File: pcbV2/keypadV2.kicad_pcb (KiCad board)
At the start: 2 copper layers, 73 parts, among them J1 Conn_01x02_Female, J2 USB_C_Receptacle, J3 Conn_01x03_Male, Q1 Q_NMOS_GSD, SW1 SW_Push, SW10 SW_Push, SW11 SW_Push, SW12 SW_Push, SW13 SW_SPDT, SW14 SW_Push, SW15 SW_Push, SW16 SW_Push, SW17 SW_DIP_x03, SW2 SW_Push, SW3 SW_Push, SW4 SW_Push, SW5 SW_Push, SW6 SW_Push, SW7 SW_Push, SW8 SW_Push, SW9 SW_Push, U1 Teensy4.0, U2 Waveshare_OLED_RGB

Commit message: remade teensy footprint
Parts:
- J2: moved to B.Cu
- U1: footprint teensy:Teensy40 -> teensy:Teensy40_REDUCED_PINS
- moved C13 148.5 mm to (264.5, 136.4)
- moved C8 148.5 mm to (258.5, 163.0)
- moved D13 148.5 mm to (258.6, 136.5)
- moved D21 148.5 mm to (259.8, 158.0)
- moved D9 148.5 mm to (279.4, 164.0)
- moved SW13 148.5 mm to (253.2, 157.0)
- moved SW16 148.5 mm to (280.8, 156.8)
- moved SW17 148.5 mm to (272.7, 157.5)
- moved SW10 147.9 mm to (111.3, 178.3)
- moved SW2 122.0 mm to (91.4, 137.7)
- moved SW6 120.8 mm to (111.3, 157.5)
- moved SW11 99.8 mm to (131.1, 178.3)
- moved J2 97.0 mm to (130.3, 113.8)
- moved SW1 91.7 mm to (91.4, 117.9)
- moved J1 77.7 mm to (132.8, 119.4), turned to 90 degrees
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
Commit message: basic layout v1
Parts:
- D1, D10, D11, D12, D2, D3, D4, D5, D6, D7, D8, D9, J1, SW14, SW15, SW16, SW17: moved to B.Cu
- moved SW13 219.6 mm to (34.3, 173.3)
- moved D13 216.9 mm to (42.2, 121.3)
- moved R2 196.8 mm to (82.5, 75.2)
- moved D9 196.5 mm to (83.1, 171.7), turned to 270 degrees
- moved D1 196.2 mm to (83.1, 111.3), turned to 270 degrees
- moved R5 193.4 mm to (83.8, 62.7)
- moved R4 187.6 mm to (63.6, 114.1)
- moved R3 186.8 mm to (73.5, 114.0)
- moved D10 182.2 mm to (102.9, 171.7), turned to 270 degrees
- moved D5 181.8 mm to (83.1, 150.9), turned to 270 degrees
- moved D11 170.2 mm to (122.7, 171.7), turned to 270 degrees
- moved R1 168.9 mm to (68.3, 128.5)
- moved D7 161.7 mm to (122.7, 150.9), turned to 270 degrees
- moved D2 160.1 mm to (83.1, 131.1), turned to 270 degrees
- moved Q1 156.5 mm to (125.5, 69.7)
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
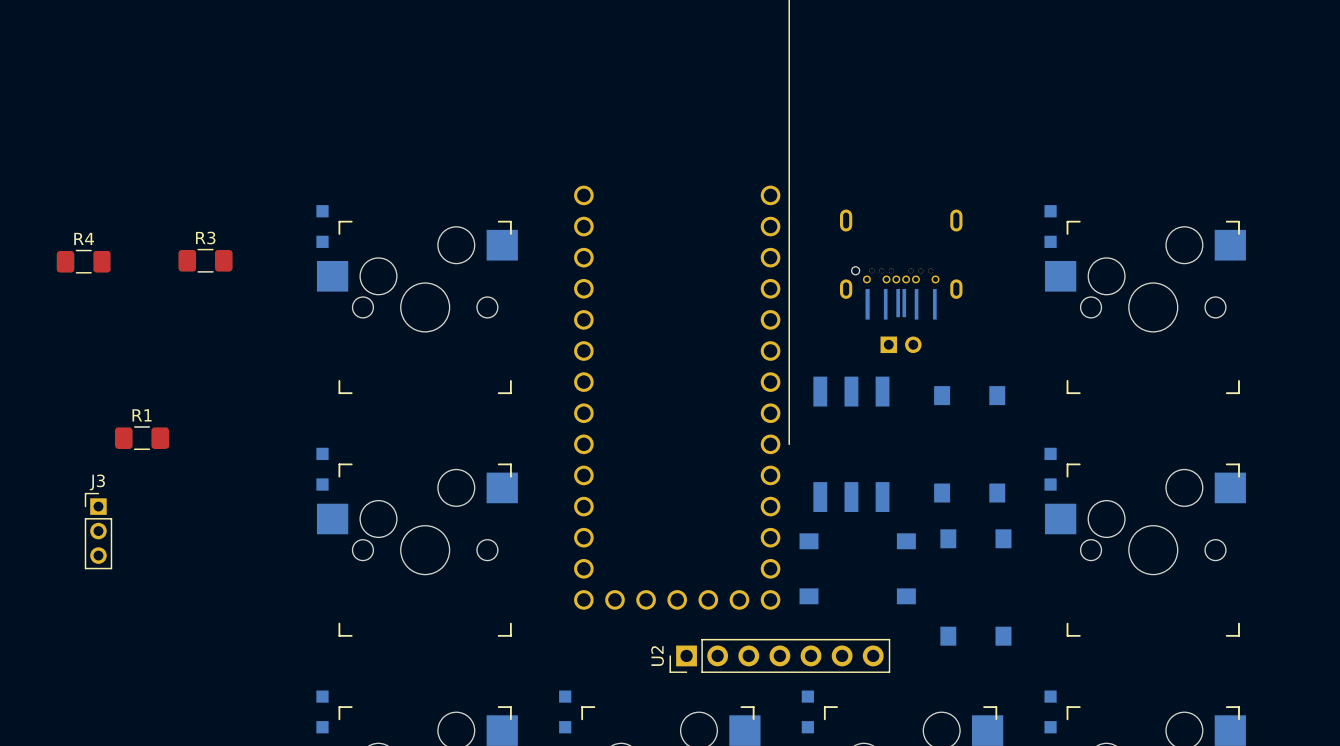
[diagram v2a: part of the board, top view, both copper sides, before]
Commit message: created footprint for lcd
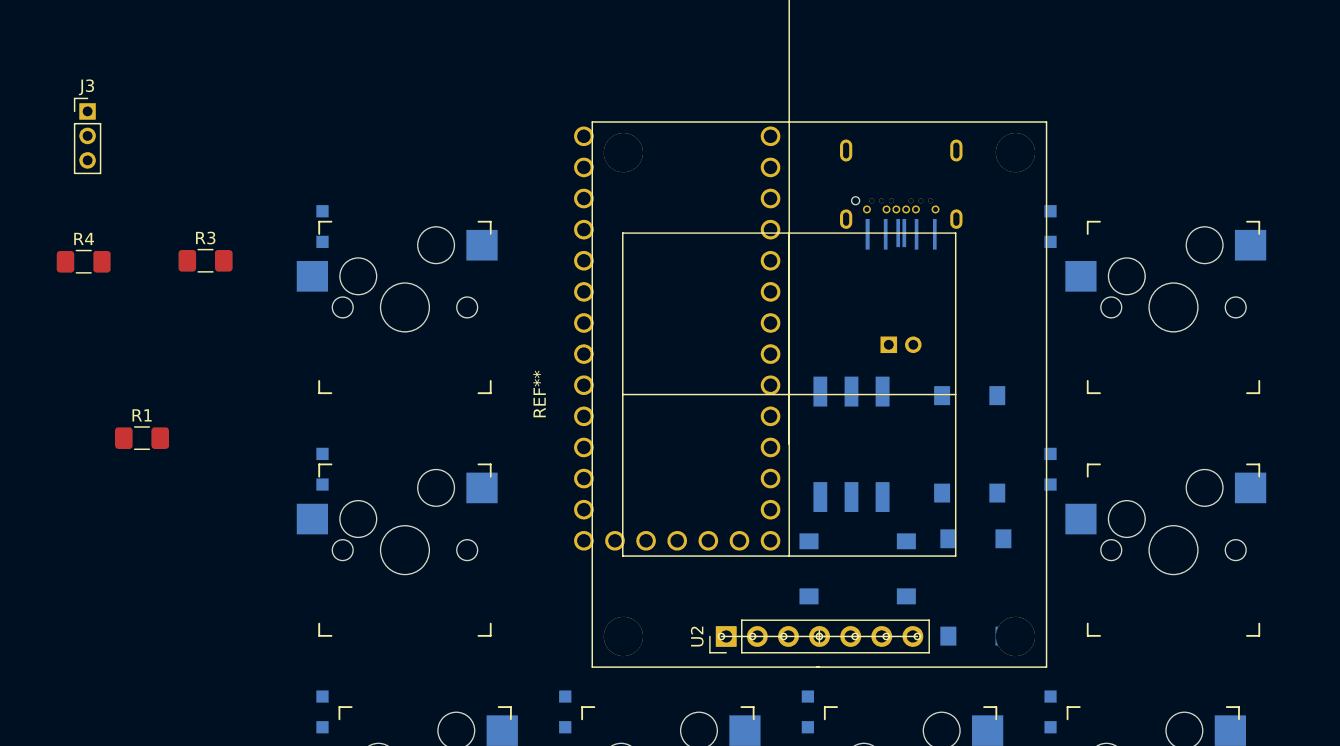
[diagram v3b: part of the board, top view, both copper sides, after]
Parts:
- added REF**: Waveshare_LCD_mount V2, custom:Waveshare_LCD_mount V2, F.Cu at (121.2, 125.0)
- moved J3 32.3 mm to (63.9, 101.9)
- moved J2 5.72 mm to (130.3, 108.1)
- moved U1 4.83 mm to (112.0, 120.4)
- moved U2 3.61 mm to (116.0, 144.7)
- moved SW1 1.65 mm to (89.8, 117.9)
- moved SW2 1.65 mm to (89.8, 137.7)
- moved SW3 1.65 mm to (152.5, 137.7)
- moved SW4 1.65 mm to (152.5, 117.9)
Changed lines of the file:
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@@
     (tracks 0)
     (zones 0)
-    (modules 73)
+    (modules 74)
     (nets 77)
   )
@@
     (add_net USB_VBUS)
   )
+  (module "custom:Waveshare_LCD_mount V2" (layer F.Cu)
+    (at 121.158 124.968 270)
+    (fp_text reference REF** (at 0 20.3374 90) (layer F.SilkS)
+      (effects (font (size 1 1) (thickness 0.15)))
+    )
+    (fp_text value "Waveshare_LCD_mount V2" (at 0 19.3374 90) (layer F.Fab)
+      (effects (font (size 1 1) (thickness 0.15)))
+    )
+    (fp_line (start 19.7485 -2.4638) (end 19.7485 -1.9431) (layer F.SilkS) (width 0.12))
+    (fp_line (start 19.7485 -2.4638) (end 19.7485 -2.9845) (layer F.SilkS) (width 0.12))
+    (fp_line (start 19.7485 -2.4638) (end 20.2692 -2.4638) (layer F.SilkS) (width 0.12))
+    (fp_line (start 19.7485 -2.4638) (end 19.2278 -2.4638) (layer F.SilkS) (width 0.12))
+    (fp_circle (center 19.7485 -2.4638) (end 20.0025 -2.4638) (layer F.SilkS) (width 0.12))
+    (fp_circle (center 19.7485 -5.3848) (end 20.0025 -5.3848) (layer F.SilkS) (width 0.12))
+    (fp_circle (center 19.7485 0.4572) (end 20.0025 0.4572) (layer F.SilkS) (width 0.12))
+    (fp_line (start 19.7485 0.4572) (end 19.7485 -2.0828) (layer F.SilkS) (width 0.12))
+    (fp_line (start 19.7485 -2.8448) (end 19.7485 -5.3848) (layer F.SilkS) (width 0.12))
+    (fp_line (start 19.7485 -5.3848) (end 19.7485 -7.9248) (layer F.SilkS) (width 0.12))
+    (fp_line (start 19.7485 0.4572) (end 19.7485 2.9972) (layer F.SilkS) (width 0.12))
+    (fp_circle (center 19.7485 2.9972) (end 20.0025 2.9972) (layer F.SilkS) (width 0.12))
+    (fp_circle (center 19.7485 -7.9248) (end 20.0025 -7.9248) (layer F.SilkS) (width 0.12))
+    (fp_line (start 19.7485 -10.4648) (end 19.7485 -7.9248) (layer F.SilkS) (width 0.12))
+    (fp_line (start 19.7485 5.5372) (end 19.7485 2.9972) (layer F.SilkS) (width 0.12))
+    (fp_line (start 0 -13.589) (end 0 13.589) (layer F.SilkS) (width 0.12))
+    (fp_line (start 22.2504 -2.4638) (end 22.2504 -2.2606) (layer F.SilkS) (width 0.12))
+    (fp_line (start 13.1826 -13.589) (end -13.1826 -13.589) (layer F.SilkS) (width 0.12))
+    (fp_line (start -22.2504 -21.0058) (end -22.2504 16.0782) (layer F.SilkS) (width 0.12))
+    (fp_line (start 22.2504 -21.0058) (end -22.2504 -21.0058) (layer F.SilkS) (width 0.12))
+    (fp_circle (center 19.7485 5.5372) (end 20.0025 5.5372) (layer F.SilkS) (width 0.12))
+    (fp_line (start 22.2504 -21.0058) (end 22.2504 16.0782) (layer F.SilkS) (width 0.12))
+    (fp_line (start 22.2504 16.0782) (end -22.2504 16.0782) (layer F.SilkS) (width 0.12))
+    (fp_circle (center 19.7485 -10.4648) (end 20.0025 -10.4648) (layer F.SilkS) (width 0.12))
+    (fp_line (start 13.1826 13.589) (end -13.1826 13.589) (layer F.SilkS) (width 0.12))
+    (fp_line (start 13.1826 0) (end -13.1826 0) (layer F.SilkS) (width 0.12))
+    (fp_line (start 13.1826 -13.589) (end 13.1826 13.589) (layer F.SilkS) (width 0.12))
+    (fp_line (start -13.1826 -13.589) (end -13.1826 13.589) (layer F.SilkS) (width 0.12))
+    (pad 1 thru_hole circle (at 19.7485 13.5382 270) (size 3.2 3.2) (drill 3.2) (layers *.Cu *.Mask))
+    (pad 2 thru_hole circle (at -19.7485 13.5382 270) (size 3.2 3.2) (drill 3.2) (layers *.Cu *.Mask))
+    (pad 3 thru_hole circle (at -19.7485 -18.4658 270) (size 3.2 3.2) (drill 3.2) (layers *.Cu *.Mask))
+    (pad 4 thru_hole circle (at 19.7485 -18.4658 270) (size 3.2 3.2) (drill 3.2) (layers *.Cu *.Mask))
+  )
   (module Capacitor_SMD:C_1206_3216Metric_Pad1.42x1.75mm_HandSolder (layer F.Cu)
     (at 262.981001 81.025001)
@@
   )
   (module custom:USB_C_REDUCED_UJ31-CH-G2 (layer B.Cu)
-    (at 130.302 113.792)
+    (at 130.302 108.077)
     (fp_text reference J2 (at 0.0508 -0.508) (layer B.SilkS)
       (effects (font (size 1 1) (thickness 0.15)) (justify mirror))
@@
   )
   (module Connector_PinHeader_2.00mm:PinHeader_1x03_P2.00mm_Vertical (layer F.Cu)
-    (at 64.77 134.112)
+    (at 63.881 101.854)
     (descr "Through hole straight pin header, 1x03, 2.00mm pitch, single row")
     (tags "Through hole pin header THT 1x03 2.00mm single row")
@@
   )
   (module keyswitches:Kailh_socket_MX (layer F.Cu)
-    (at 91.44 117.856)
+    (at 89.789 117.856)
     (descr "MX-style keyswitch with Kailh socket mount")
     (tags MX,cherry,gateron,kailh,pg1511,socket)
@@
   )
   (module keyswitches:Kailh_socket_MX (layer F.Cu)
-    (at 91.44 137.668)
+    (at 89.789 137.668)
     (descr "MX-style keyswitch with Kailh socket mount")
     (tags MX,cherry,gateron,kailh,pg1511,socket)
@@
   )
   (module keyswitches:Kailh_socket_MX (layer F.Cu)
-    (at 150.876 137.668)
+    (at 152.527 137.668)
     (descr "MX-style keyswitch with Kailh socket mount")
     (tags MX,cherry,gateron,kailh,pg1511,socket)
@@
   )
   (module keyswitches:Kailh_socket_MX (layer F.Cu)
-    (at 150.876 117.856)
+    (at 152.527 117.856)
     (descr "MX-style keyswitch with Kailh socket mount")
     (tags MX,cherry,gateron,kailh,pg1511,socket)
@@
   )
   (module Connector_PinHeader_2.54mm:PinHeader_1x07_P2.54mm_Vertical (layer F.Cu)
-    (at 112.776 146.304 90)
+    (at 116.0145 144.7165 90)
     (descr "Through hole straight pin header, 1x07, 2.54mm pitch, single row")
     (tags "Through hole pin header THT 1x07 2.54mm single row")
@@
       (effects (font (size 1 1) (thickness 0.15)))
     )
-    (fp_line (start -0.635 -1.27) (end 1.27 -1.27) (layer F.Fab) (width 0.1))
-    (fp_line (start 1.27 -1.27) (end 1.27 16.51) (layer F.Fab) (width 0.1))
-    (fp_line (start 1.27 16.51) (end -1.27 16.51) (layer F.Fab) (width 0.1))
-    (fp_line (start -1.27 16.51) (end -1.27 -0.635) (layer F.Fab) (width 0.1))
-    (fp_line (start -1.27 -0.635) (end -0.635 -1.27) (layer F.Fab) (width 0.1))
-    (fp_line (start -1.33 16.57) (end 1.33 16.57) (layer F.SilkS) (width 0.12))
-    (fp_line (start -1.33 1.27) (end -1.33 16.57) (layer F.SilkS) (width 0.12))
-    (fp_line (start 1.33 1.27) (end 1.33 16.57) (layer F.SilkS) (width 0.12))
-    (fp_line (start -1.33 1.27) (end 1.33 1.27) (layer F.SilkS) (width 0.12))
-    (fp_line (start -1.33 0) (end -1.33 -1.33) (layer F.SilkS) (width 0.12))
-    (fp_line (start -1.33 -1.33) (end 0 -1.33) (layer F.SilkS) (width 0.12))
-    (fp_line (start -1.8 -1.8) (end -1.8 17.05) (layer F.CrtYd) (width 0.05))
-    (fp_line (start -1.8 17.05) (end 1.8 17.05) (layer F.CrtYd) (width 0.05))
-    (fp_line (start 1.8 17.05) (end 1.8 -1.8) (layer F.CrtYd) (width 0.05))
-    (fp_line (start 1.8 -1.8) (end -1.8 -1.8) (layer F.CrtYd) (width 0.05))
     (fp_text user %R (at 0 7.62) (layer F.Fab)
       (effects (font (size 1 1) (thickness 0.15)))
     )
-    (pad 1 thru_hole rect (at 0 0 90) (size 1.7 1.7) (drill 1) (layers *.Cu *.Mask)
-      (net 2 +5V))
-    (pad 2 thru_hole oval (at 0 2.54 90) (size 1.7 1.7) (drill 1) (layers *.Cu *.Mask)
-      (net 1 GND))
-    (pad 3 thru_hole oval (at 0 5.08 90) (size 1.7 1.7) (drill 1) (layers *.Cu *.Mask)
-      (net 70 MOSI))
-    (pad 4 thru_hole oval (at 0 7.62 90) (size 1.7 1.7) (drill 1) (layers *.Cu *.Mask)
-      (net 62 SCK))
-    (pad 5 thru_hole oval (at 0 10.16 90) (size 1.7 1.7) (drill 1) (layers *.Cu *.Mask)
-      (net 71 CS))
-    (pad 6 thru_hole oval (at 0 12.7 90) (size 1.7 1.7) (drill 1) (layers *.Cu *.Mask)
-      (net 72 DISP_DC))
+    (fp_line (start 1.8 -1.8) (end -1.8 -1.8) (layer F.CrtYd) (width 0.05))
+    (fp_line (start 1.8 17.05) (end 1.8 -1.8) (layer F.CrtYd) (width 0.05))
+    (fp_line (start -1.8 17.05) (end 1.8 17.05) (layer F.CrtYd) (width 0.05))
+    (fp_line (start -1.8 -1.8) (end -1.8 17.05) (layer F.CrtYd) (width 0.05))
+    (fp_line (start -1.33 -1.33) (end 0 -1.33) (layer F.SilkS) (width 0.12))
+    (fp_line (start -1.33 0) (end -1.33 -1.33) (layer F.SilkS) (width 0.12))
+    (fp_line (start -1.33 1.27) (end 1.33 1.27) (layer F.SilkS) (width 0.12))
+    (fp_line (start 1.33 1.27) (end 1.33 16.57) (layer F.SilkS) (width 0.12))
+    (fp_line (start -1.33 1.27) (end -1.33 16.57) (layer F.SilkS) (width 0.12))
+    (fp_line (start -1.33 16.57) (end 1.33 16.57) (layer F.SilkS) (width 0.12))
+    (fp_line (start -1.27 -0.635) (end -0.635 -1.27) (layer F.Fab) (width 0.1))
+    (fp_line (start -1.27 16.51) (end -1.27 -0.635) (layer F.Fab) (width 0.1))
+    (fp_line (start 1.27 16.51) (end -1.27 16.51) (layer F.Fab) (width 0.1))
+    (fp_line (start 1.27 -1.27) (end 1.27 16.51) (layer F.Fab) (width 0.1))
+    (fp_line (start -0.635 -1.27) (end 1.27 -1.27) (layer F.Fab) (width 0.1))
     (pad 7 thru_hole oval (at 0 15.24 90) (size 1.7 1.7) (drill 1) (layers *.Cu *.Mask)
       (net 73 DISP_RST))
+    (pad 6 thru_hole oval (at 0 12.7 90) (size 1.7 1.7) (drill 1) (layers *.Cu *.Mask)
+      (net 72 DISP_DC))
+    (pad 5 thru_hole oval (at 0 10.16 90) (size 1.7 1.7) (drill 1) (layers *.Cu *.Mask)
+      (net 71 CS))
+    (pad 4 thru_hole oval (at 0 7.62 90) (size 1.7 1.7) (drill 1) (layers *.Cu *.Mask)
+      (net 62 SCK))
+    (pad 3 thru_hole oval (at 0 5.08 90) (size 1.7 1.7) (drill 1) (layers *.Cu *.Mask)
+      (net 70 MOSI))
+    (pad 2 thru_hole oval (at 0 2.54 90) (size 1.7 1.7) (drill 1) (layers *.Cu *.Mask)
+      (net 1 GND))
+    (pad 1 thru_hole rect (at 0 0 90) (size 1.7 1.7) (drill 1) (layers *.Cu *.Mask)
+      (net 2 +5V))
     (model ${KISYS3DMOD}/Connector_PinHeader_2.54mm.3dshapes/PinHeader_1x07_P2.54mm_Vertical.wrl
       (at (xyz 0 0 0))
@@
   )
   (module teensy:Teensy40_REDUCED_PINS (layer F.Cu)
-    (at 112.014 125.222 270)
+    (at 112.014 120.396 270)
     (fp_text reference U1 (at 0 10.3632 270) (layer B.SilkS)
       (effects (font (size 1 1) (thickness 0.15)) (justify mirror))

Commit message: basic layout v1
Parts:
- Q1, R2, R3, R4: moved to B.Cu
- SW1, SW10, SW11, SW12, SW2, SW3, SW4, SW5, SW6, SW7, SW8, SW9: footprint keyswitches:Kailh_socket_MX -> keyswitches:Kailh_socket_MX_RGB_cutout
- moved R4 60.3 mm to (123.2, 105.3), turned to 90 degrees
- moved Q1 47.5 mm to (100.3, 110.0), turned to 270 degrees
- moved J3 40.0 mm to (99.1, 120.9)
- moved R5 36.0 mm to (111.6, 85.5)
- moved R2 35.9 mm to (100.1, 106.6)
- moved R3 26.8 mm to (100.3, 114.7), turned to 90 degrees
- moved D1 1.78 mm to (81.3, 111.3)
- moved D2 1.78 mm to (81.3, 131.1)
- moved D3 1.52 mm to (144.0, 131.1)
- moved D4 1.52 mm to (144.0, 111.3)
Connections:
- Q1 pad 3: Net-(Q1-Pad3) -> RGB_DIN
- R3 pad 2: Net-(Q1-Pad3) -> RGB_DIN
- R5 pad 2: Net-(Q1-Pad3) -> RGB_DIN

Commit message: edge cuts
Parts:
- added REF**: MountingHole_2.7mm_M2.5, MountingHole:MountingHole_2.7mm_M2.5, F.Cu at (78.7, 189.4)
- added REF**: MountingHole_2.7mm_M2.5, MountingHole:MountingHole_2.7mm_M2.5, F.Cu at (163.6, 189.4)
- added REF**: MountingHole_2.7mm_M2.5, MountingHole:MountingHole_2.7mm_M2.5, F.Cu at (163.6, 106.8)
- added REF**: MountingHole_3.2mm_M3, MountingHole:MountingHole_3.2mm_M3, F.Cu at (78.7, 106.8)
- moved SW13 157.6 mm to (184.9, 127.0)
- moved J2 0.89 mm to (130.3, 107.2)
- moved U1 0.89 mm to (112.0, 119.5)
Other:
- board outline added: 93.7 x 93.3 mm
